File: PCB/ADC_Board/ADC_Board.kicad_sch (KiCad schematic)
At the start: 18 parts, among them U1 ADAU1979xBCP, U2 STM32H750VBTx

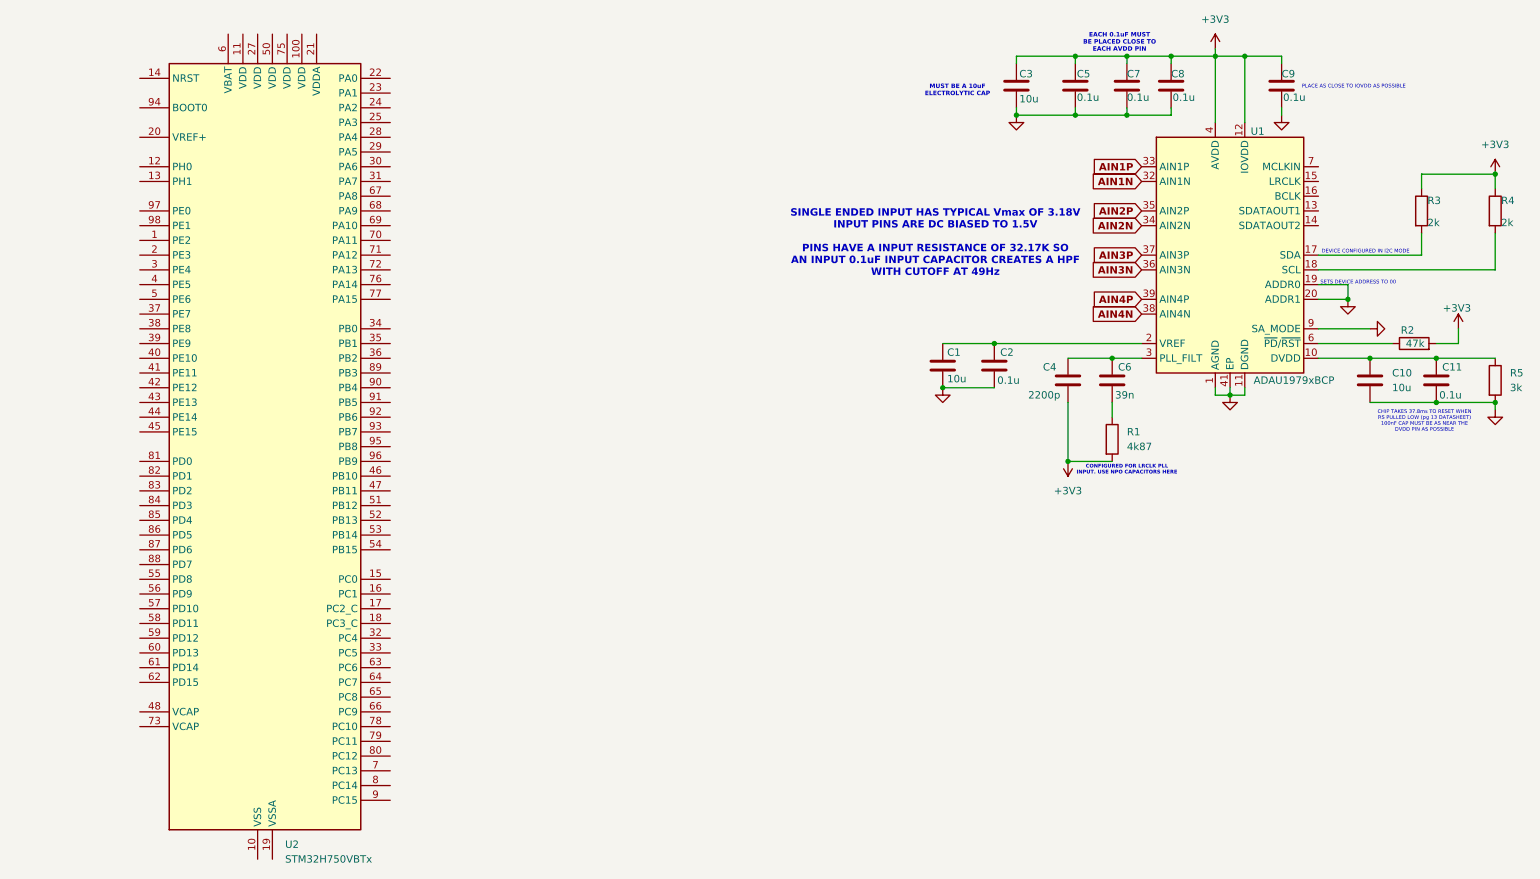
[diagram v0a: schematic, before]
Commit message: Updated File Layout
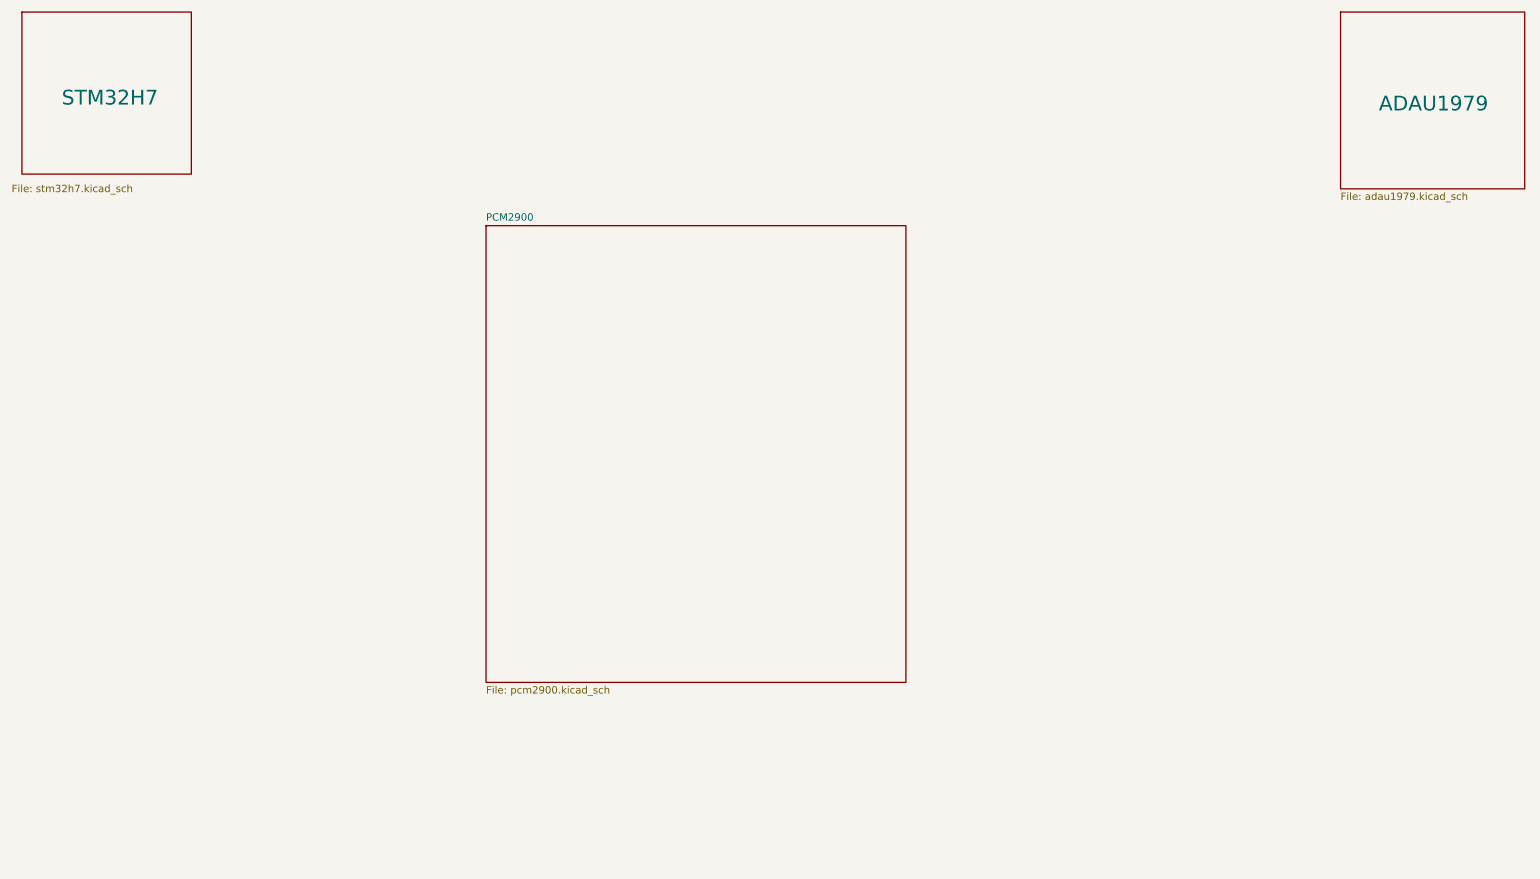
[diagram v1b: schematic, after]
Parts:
- removed C1, C10, C3: 10u, symbol Device:C
- removed C11, C2, C5, C7, C8, C9: 0.1u, symbol Device:C
- removed C4: 2200p, symbol Device:C
- removed C6: 39n, symbol Device:C
- removed R1: 4k87, symbol Device:R
- removed R2: 47k, symbol Device:R
- removed R3, R4: 2k, symbol Device:R
- removed R5: 3k, symbol Device:R
- removed U1: ADAU1979xBCP, Package_CSP:LFCSP-40-1EP_6x6mm_P0.5mm_EP3.9x3.9mm, symbol Audio:ADAU1979xBCP
- removed U2: STM32H750VBTx, Package_QFP:LQFP-100_14x14mm_P0.5mm, symbol MCU_ST_STM32H7:STM32H750VBTx
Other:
- added sheet ADAU1979 (adau1979.kicad_sch)
- added sheet PCM2900 (pcm2900.kicad_sch)
- added sheet STM32H7 (stm32h7.kicad_sch)
- note removed: "CHIP TAKES 37.8ms TO RESET WHEN RS PULLED LOW (pg 13 DATASHEET) 100nF CAP MUST BE AS NEAR THE DVDD PIN AS POSSIBLE"
- note removed: "CONFIGURED FOR LRCLK PLL INPUT. USE NPO CAPACITORS HERE"
- note removed: "DEVICE CONFIGURED IN I2C MODE"
- note removed: "EACH 0.1uF MUST BE PLACED CLOSE TO EACH AVDD PIN"
- note removed: "MUST BE A 10uF ELECTROLYTIC CAP"
- note removed: "PLACE AS CLOSE TO IOVDD AS POSSIBLE"
- note removed: "SETS DEVICE ADDRESS TO 00"
- note removed: "SINGLE ENDED INPUT HAS TYPICAL Vmax OF 3.18V INPUT PINS ARE DC BIASED TO 1.5V PINS HAVE A INPUT RESISTANCE OF 32.17K SO AN INPUT 0.1uF INPUT CAPACITOR CREATES A HPF WITH CUTOFF AT 49Hz"
